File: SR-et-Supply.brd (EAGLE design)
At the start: 28.9 x 16.5 mm, 14 parts

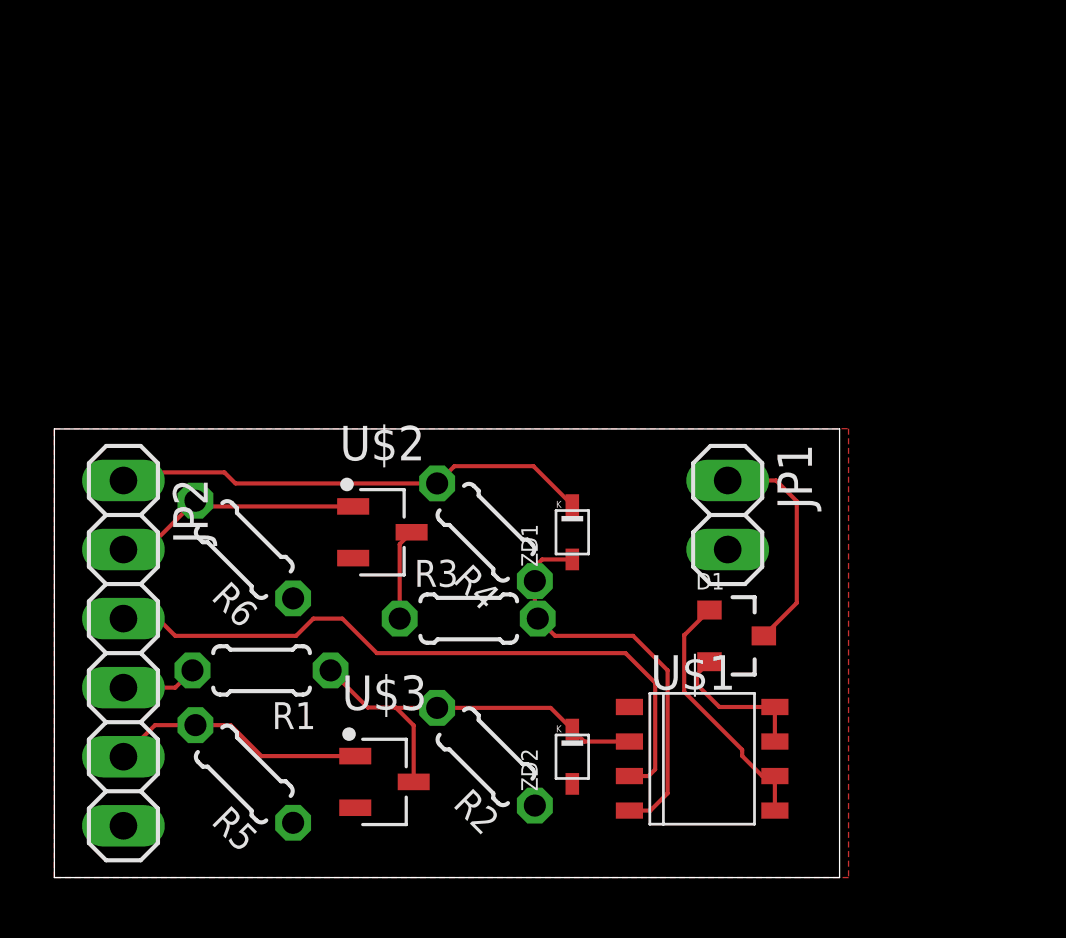
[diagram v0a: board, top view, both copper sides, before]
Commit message: Make Source Follwer FET derived from the existing test board to SR-et-Supply, and added ShiftResistor to it
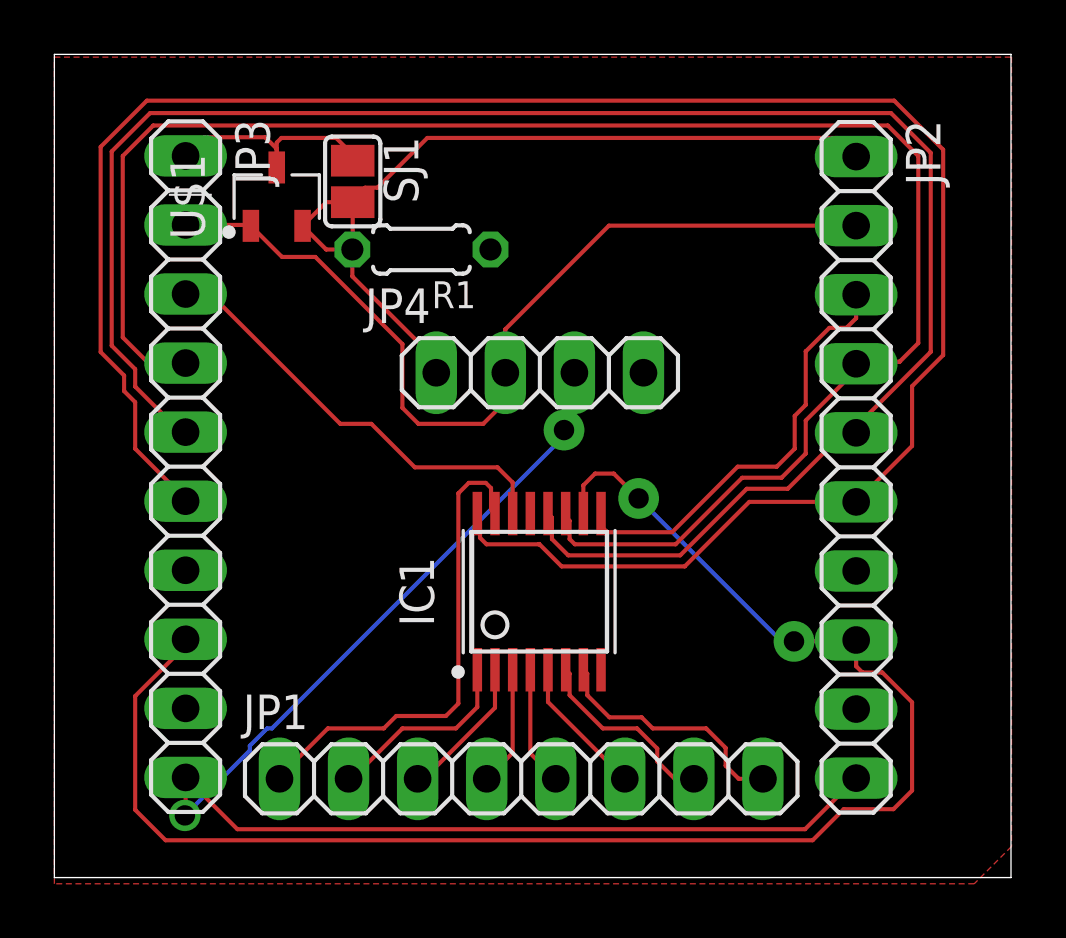
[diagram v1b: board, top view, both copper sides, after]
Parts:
- removed D1: GSD2004S, Diode_Vishay:SOT23
- removed R2, R4, R5, R6: 103, rcl:0204/5
- removed R3: 104, rcl:0204/5
- removed U$2: 2SK3072-TB-E, Transistor-FET:SOT95P250X120-3
- removed U$3: IRLML6344TRPBFTR, Transistor-FET:SOT95P250X120-3
- removed ZD1, ZD2: MM5Z15V, fairchild-semic:SOD523
- added IC1: 74595PW, 74xx-eu:TTSOP16
- added JP3: (no value), pinhead:1X10
- added JP4: (no value), pinhead:1X04
- added SJ1: (no value), jumper:SJ
- JP1: device pinhead:1X02 -> pinhead:1X08
- JP2: device pinhead:1X06 -> pinhead:1X10
- R1: value 103 -> 105
- U$1: value TC1550TG -> 2SK3072-TB-E; device TC1550:SOIC-08LG -> Transistor-FET:SOT95P250X120-3
- moved JP2 27.8 mm to (29.5, 15.1)
- moved U$1 25.9 mm to (8.18, 25.0), turned to 90 degrees
- moved R1 16.6 mm to (13.5, 23.1)
- moved JP1 12.3 mm to (17.2, 3.63), turned to 0 degrees
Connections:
- removed net VDD: JP2.1, R4.2, ZD1.P$1
- new net +5V: IC1.16, JP2.6, JP3.6
- new net 300V: JP3.1, SJ1.1, U$1.3
- new net CLR: IC1.10, JP2.8, JP3.8
- new net OFLOW: IC1.9, JP2.3
- new net RCK: IC1.12, JP2.5, JP3.5
- new net SCK: IC1.11, JP2.4, JP3.4
- new net SER: IC1.14, JP3.3
- new net VPPCLONE: JP2.1, JP4.1, R1.2, SJ1.2, U$1.2
- net +12V: now also JP2.10, JP3.10, JP4.3; no longer JP2.4, R1.2
- net GND: now also IC1.13, IC1.8, JP2.7, JP3.7, JP4.4, R1.1; no longer JP1.2, JP2.6, R2.1, R5.1, R6.1, U$1.1, U$2.2, U$3.2, ZD2.P$2
- net N$1: now also IC1.15, JP1.1; no longer R1.1, R2.2, U$1.2, U$3.3, ZD2.P$1
- net N$2: now also IC1.1, JP1.2; no longer R3.1, U$2.3
- net N$3: now also IC1.2, JP1.3; no longer R3.2, R4.1, U$1.4, ZD1.P$2
- net N$4: now also IC1.3, JP1.4; no longer JP2.5, R5.2, U$3.1
- net N$5: now also IC1.4, JP1.5; no longer JP2.2, R6.2, U$2.1
- net N$7: now also IC1.5, JP1.6; no longer D1.1, U$1.5, U$1.6
- net N$8: now also IC1.6, JP1.7; no longer D1.2, U$1.7, U$1.8
- net N$9: now also IC1.7, JP1.8; no longer D1.3, JP1.1
- net VPP: now also JP2.2, JP3.2, JP4.2, U$1.1; no longer JP2.3, U$1.3
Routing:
- net +5V: track 0.00 -> 77.2 mm
- net RCK: track 0.00 -> 68.6 mm
- net SCK: track 0.00 -> 64.3 mm
- net CLR: track 0.00 -> 57.5 mm, vias 0 -> 2
- net +12V: track 2.80 -> 50.0 mm, vias 0 -> 2
- net VPPCLONE: track 0.00 -> 31.8 mm
- net VDD: track 17.7 -> 0.00 mm
- net OFLOW: track 0.00 -> 16.1 mm
- net SER: track 0.00 -> 16.0 mm
- net N$3: track 15.2 -> 5.33 mm
- net 300V: track 0.00 -> 8.76 mm
- net VPP: track 25.3 -> 33.6 mm
- net N$5: track 9.59 -> 4.40 mm
- net N$4: track 9.50 -> 4.41 mm
- net N$7: track 9.43 -> 5.18 mm
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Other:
- board size 28.9 x 16.5 mm -> 35.2 x 30.3 mm
